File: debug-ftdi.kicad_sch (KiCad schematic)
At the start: 116 parts, among them J3 USB-C_USB4105-GF-A, J4 HDMI-A_WE_685119134923, J5 MicroSD_693071020811, Q4 BSS138PW, Q5 BSS138PW, Q6 BSS138PW, Q7 BSS138PW, Q8 BSS138PW, U10 TPD4E05U06QDQARQ1, U11 TPD4E05U06QDQARQ1, U12 TPD4E05U06QDQARQ1, U13 TXU0304BQAR, U14 TPD4E05U06QDQARQ1, U5 NCP718BSN330T1G, U6 FT4232H_VQFN, U7 TXU0304BQAR, U8 TPD4E05U06QDQARQ1, U9 SN74HC595B, Y1 Resonator_12MHz_ABM8G

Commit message: Finish creating hierarchical buses and structure, start reconnecting signals
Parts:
- removed C126: C_10u_6.3V_0402, sodimm-ddr5-tester-footprints:C_0402_1005Metric, symbol sodimm-ddr5-tester:C_10u_6.3V_0402
- removed C129: C_1u_0402, sodimm-ddr5-tester-footprints:C_0402_1005Metric, symbol sodimm-ddr5-tester:C_1u_0402
- removed C132: C_100n_0402, sodimm-ddr5-tester-footprints:C_0402_1005Metric, symbol sodimm-ddr5-tester:C_100n_0402
- removed D14: BAT54-02V-G3-08, sodimm-ddr5-tester-footprints:SOD-523, symbol sodimm-ddr5-tester:BAT54-02V-G3-08
- removed D4, D5, D6, D7, D8: LED_G_0603_KP-1608CGCK, sodimm-ddr5-tester-footprints:LED_0603_1608Metric_G, symbol sodimm-ddr5-tester:LED_G_0603_KP-1608CGCK
- removed FB3: FB_120Z_2A_Murata-BLM18PG_0603, sodimm-ddr5-tester-footprints:FB_0603_1608Metric, symbol sodimm-ddr5-tester:FB_120Z_2A_Murata-BLM18PG_0603
- removed J4: HDMI-A_WE_685119134923, sodimm-ddr5-tester-footprints:HDMI-A_Receptacle_WE_685119134923, symbol sodimm-ddr5-tester:HDMI-A_WE_685119134923
- removed J5: MicroSD_693071020811, sodimm-ddr5-tester-footprints:MicroSD_Wurth_693071020811, symbol sodimm-ddr5-tester:MicroSD_693071020811
- removed Q4, Q5, Q6, Q7, Q8: BSS138PW, sodimm-ddr5-tester-footprints:SC70-3, symbol sodimm-ddr5-tester:BSS138PW
- removed R40, R41, R42, R45, R46, R84, R89: R_330R_0402, sodimm-ddr5-tester-footprints:R_0402_1005Metric, symbol sodimm-ddr5-tester:R_330R_0402
- removed R70, R71, R72, R73, R74, R75, R76, R77: R_0R_0402, sodimm-ddr5-tester-footprints:R_0402_1005Metric, symbol sodimm-ddr5-tester:R_0R_0402
- removed R80, R81, R82, R83, R85, R86, R87: R_20k_0402, sodimm-ddr5-tester-footprints:R_0402_1005Metric, symbol sodimm-ddr5-tester:R_20k_0402
- removed TP2, TP3, TP4, TP5, TP6: TP_1mm_SMD, sodimm-ddr5-tester-footprints:TP_SMD_1mm, symbol sodimm-ddr5-tester:TP_1mm_SMD
- removed U10, U11, U12, U14: TPD4E05U06QDQARQ1, sodimm-ddr5-tester-footprints:USON-10_2.5x1mm_P0.5mm, symbol sodimm-ddr5-tester:TPD4E05U06QDQARQ1
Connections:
- no-connect marks 30 -> 28
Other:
- note added: "Debug FTDI"
- note removed: "Debug UART"
- note removed: "HDMI"
- note removed: "SD card"
- note removed: "User LEDs"
- moved on the sheet: C109, C110, C111, C112, C113, C114, C115, C116, C117, C118, C119, C120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

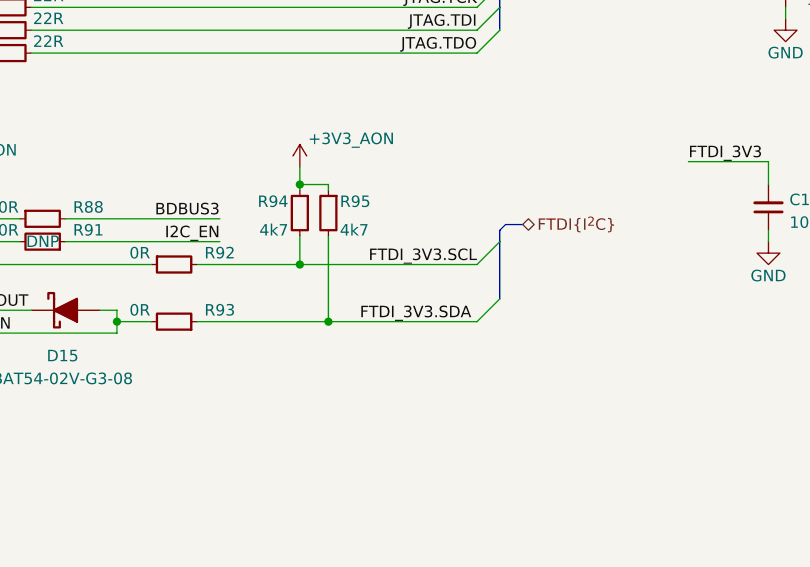
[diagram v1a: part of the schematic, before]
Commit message: Finish reconnecting signals after migration to the hierarchical structure
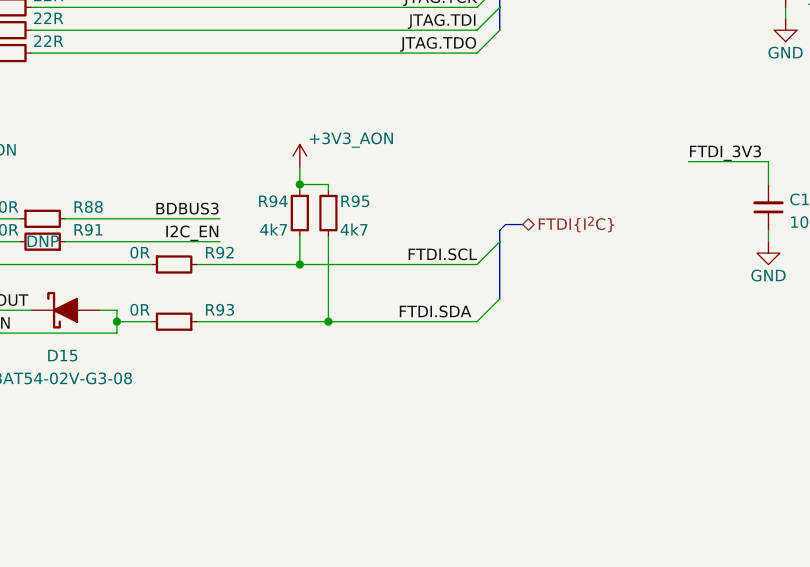
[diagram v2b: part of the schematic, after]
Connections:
- net FTDI_3V3.SCL renamed FTDI.SCL
- net FTDI_3V3.SDA renamed FTDI.SDA

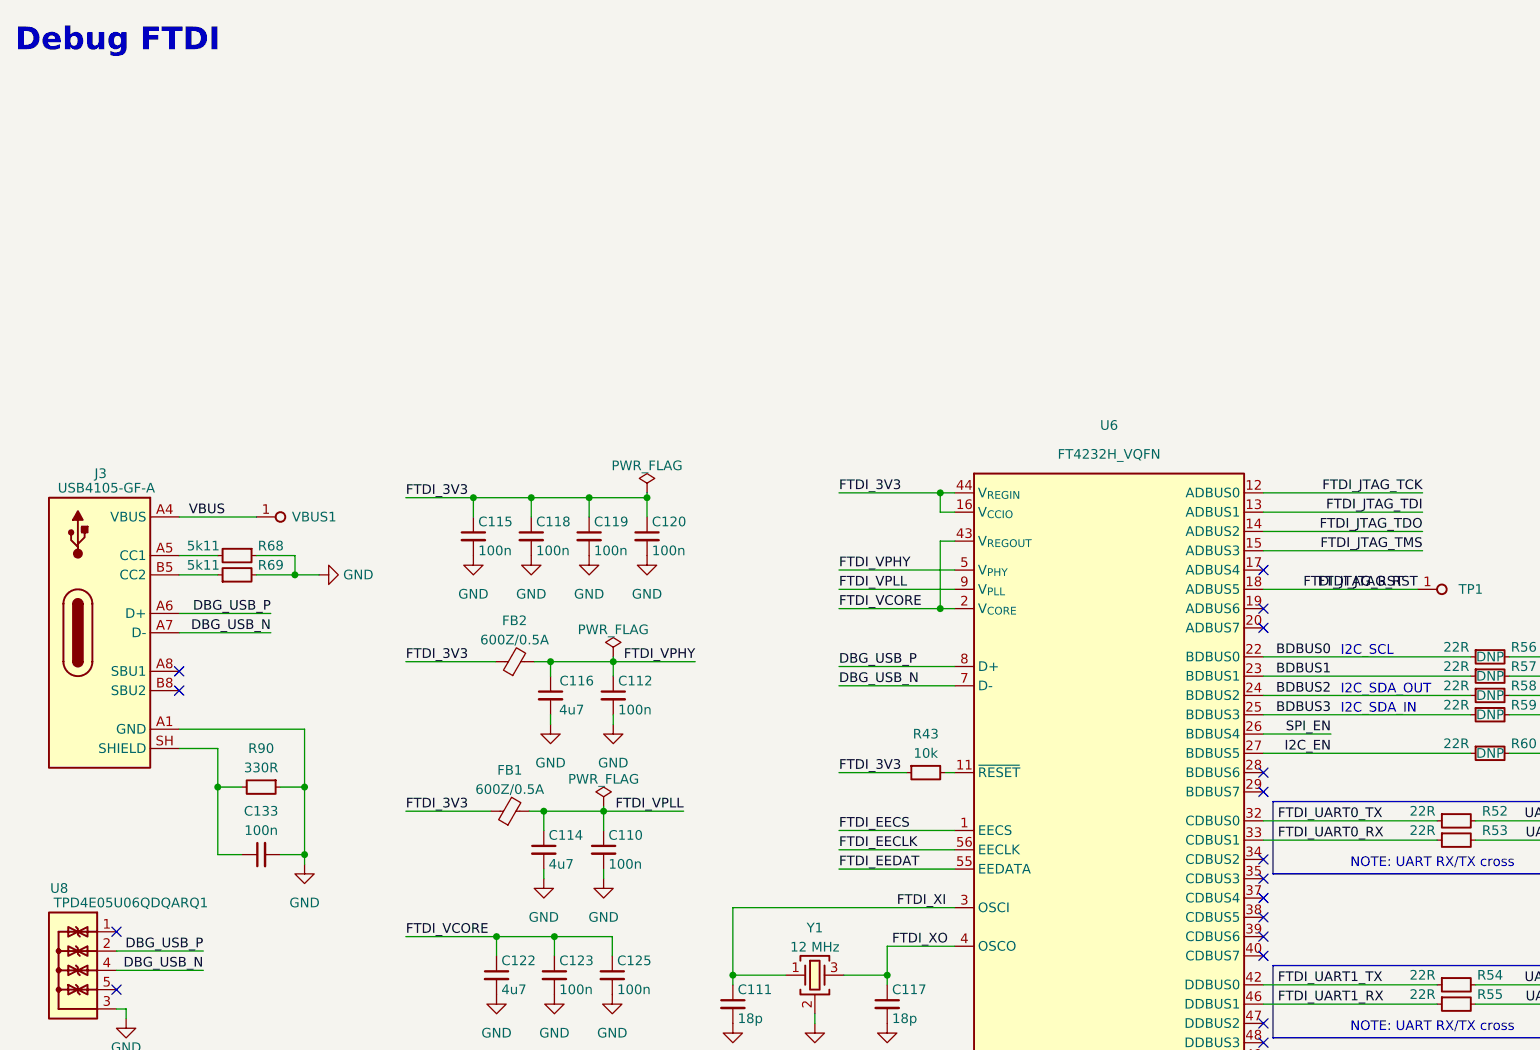
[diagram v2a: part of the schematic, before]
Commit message: Manually replace conflicted globlib files
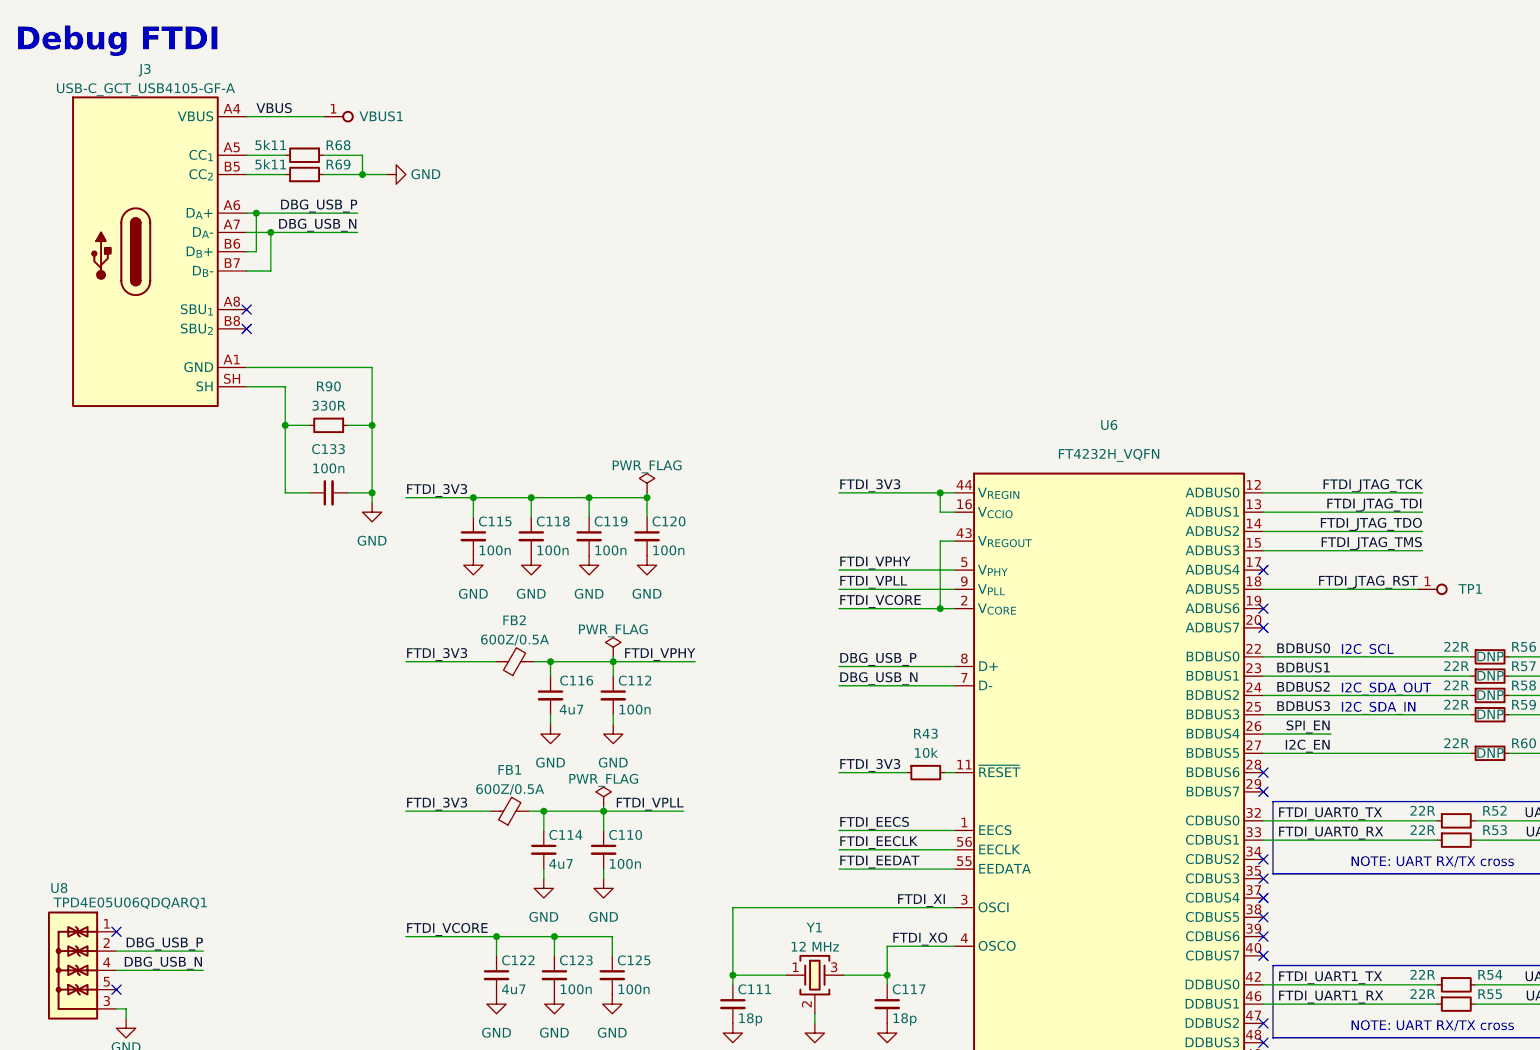
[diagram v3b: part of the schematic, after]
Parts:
- removed J3: USB-C_USB4105-GF-A, sodimm-ddr5-tester-footprints:USB-C_GCT_USB4105-GF-A, symbol sodimm-ddr5-tester:USB-C_USB4105-GF-A
- added J3: USB-C_GCT_USB4105-GF-A, antmicro-footprints:USB-C_Receptacle_GCT_USB4105-GF-A, symbol antmicroUSBConnectors:USB-C_GCT_USB4105-GF-A
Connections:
- net DBG_USB_N: now also J3.A7 (D_{A}-), J3.B7 (D_{B}-)
- net DBG_USB_P: now also J3.A6 (D_{A}+), J3.B6 (D_{B}+)
- net GND: now also J3.A1 (GND), J3.A12 (GND), J3.B1 (GND), J3.B12 (GND)
- net VBUS: now also J3.A4 (VBUS), J3.A9 (VBUS), J3.B4 (VBUS), J3.B9 (VBUS)
- net at R68.2: now also J3.A5 (CC_{1})
- net at R69.1: now also J3.B5 (CC_{2})
- net at C133.1, R90.2: now also J3.SH
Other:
- moved on the sheet: C133, R68, R69, R90, VBUS1

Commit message: Loclib of the project
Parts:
- FB1, FB2: footprint antmicro-footprints:FB_0603_1608Metric -> sodimm-ddr5-tester-footprints:FB_0603_1608Metric; symbol antmicroFerriteBeadsandChips:FB_600Z_0.5A_Murata-BLM18AG_0603 -> sodimm-ddr5-tester:FB_600Z_0.5A_Murata-BLM18AG_0603
- J3: footprint antmicro-footprints:USB-C_Receptacle_GCT_USB4105-GF-A -> sodimm-ddr5-tester-footprints:USB-C_Receptacle_GCT_USB4105-GF-A; symbol antmicroUSBConnectors:USB-C_GCT_USB4105-GF-A -> sodimm-ddr5-tester:USB-C_GCT_USB4105-GF-A
- U13: footprint sodimm-ddr5-tester-footprints:DHVQFN-14_1EP_2.5x3mm -> sodimm-ddr5-tester-footprints:DHVQFN-14-1EP_2.5x3mm
- Y1: footprint antmicro-footprints:Oscillator_SMD_Geyer_KX-7-4Pin_3.2x2.5mm -> sodimm-ddr5-tester-footprints:Oscillator_SMD_Geyer_KX-7-4Pin_3.2x2.5mm; symbol antmicroResonators:Resonator_12MHz_ABM8G -> sodimm-ddr5-tester:Resonator_12MHz_ABM8G

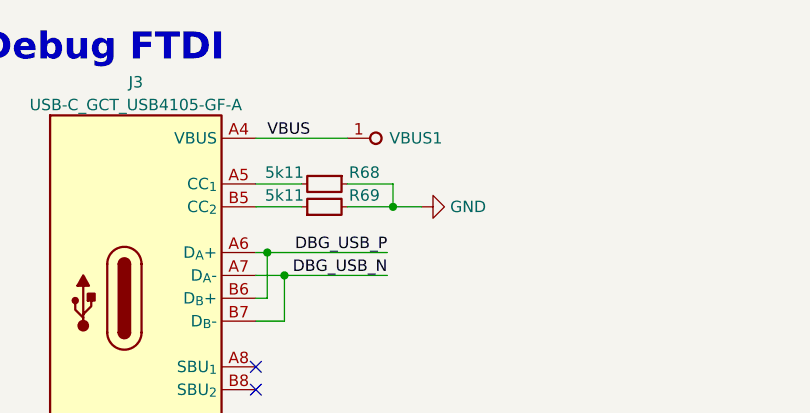
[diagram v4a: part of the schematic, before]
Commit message: Finish updating components to newest versions, improve silkscreen marking, bump revision
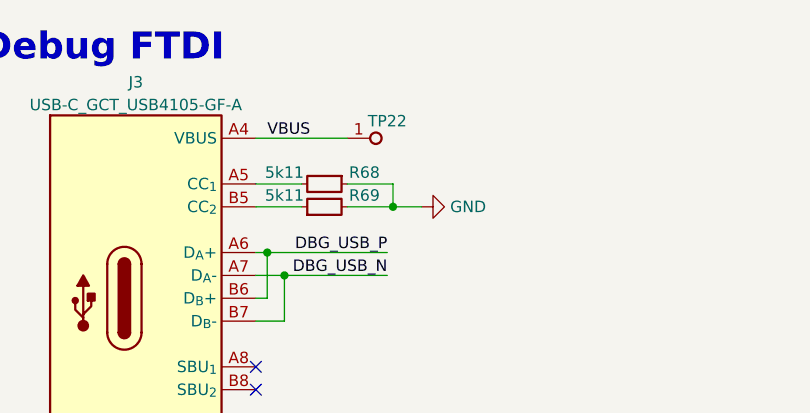
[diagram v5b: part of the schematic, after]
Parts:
- U7: footprint sodimm-ddr5-tester-footprints:DHVQFN-14_1EP_2.5x3mm -> sodimm-ddr5-tester-footprints:DHVQFN-14-1EP_2.5x3mm
- renumbered VBUS1 to TP22
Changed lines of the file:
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@@
     (title_block
         (title "SO-DIMM DDR5 Tester")
-        (date "2024-01-10")
-        (rev "1.1.0")
+        (date "2024-01-18")
+        (rev "1.1.1")
         (company "Antmicro Ltd.")
         (comment 1 "www.antmicro.com")
         (comment 2 "Antmicro Ltd"))
-    (bus_alias "SDIO"
-        (members "DAT[0..3]" "CMD" "CLK" "CD"))
-    (bus_alias "TMDS"
-        (members "D0_P" "D0_N" "D1_P" "D1_N" "D2_P" "D2_N" "CLK_P" "CLK_N"))
-    (bus_alias "USB"
-        (members "D+"))
     (junction
         (at 136.398 93.98)
@@
                     (size 1.27 1.27)
                     (thickness 0.15))))
-        (property "Footprint" "sodimm-ddr5-tester-footprints:DHVQFN-14_1EP_2.5x3mm"
+        (property "Footprint" "sodimm-ddr5-tester-footprints:DHVQFN-14-1EP_2.5x3mm"
             (id 2)
             (at 300.355 74.93 0)
@@
         (in_bom yes)
         (on_board yes)
-        (property "Reference" "VBUS1"
+        (property "Reference" "TP22"
             (id 0)
-            (at 62.865 29.21 0))
+            (at 59.69 27.305 0))
         (property "Value" "TP_1mm_SMD"
             (id 1)

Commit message: Finish schematic cleanup
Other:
- moved on the sheet: C109, C110, C111, C112, C113, C114, C115, C116, C117, C118, C119, C120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

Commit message: Clean schematic DRC
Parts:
- C111, C117: MPN MC0402N180J500CT -> CL05C180JB51PNC; Manufacturer Multicomp -> Samsung Electro-Mechanics
- U6: Manufacturer FTDI -> FTDI Chip
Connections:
- net SPI_EN: no longer names the net of U6.26 (BDBUS4)
- no-connect marks 28 -> 29
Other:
- note added: "SPI_EN"

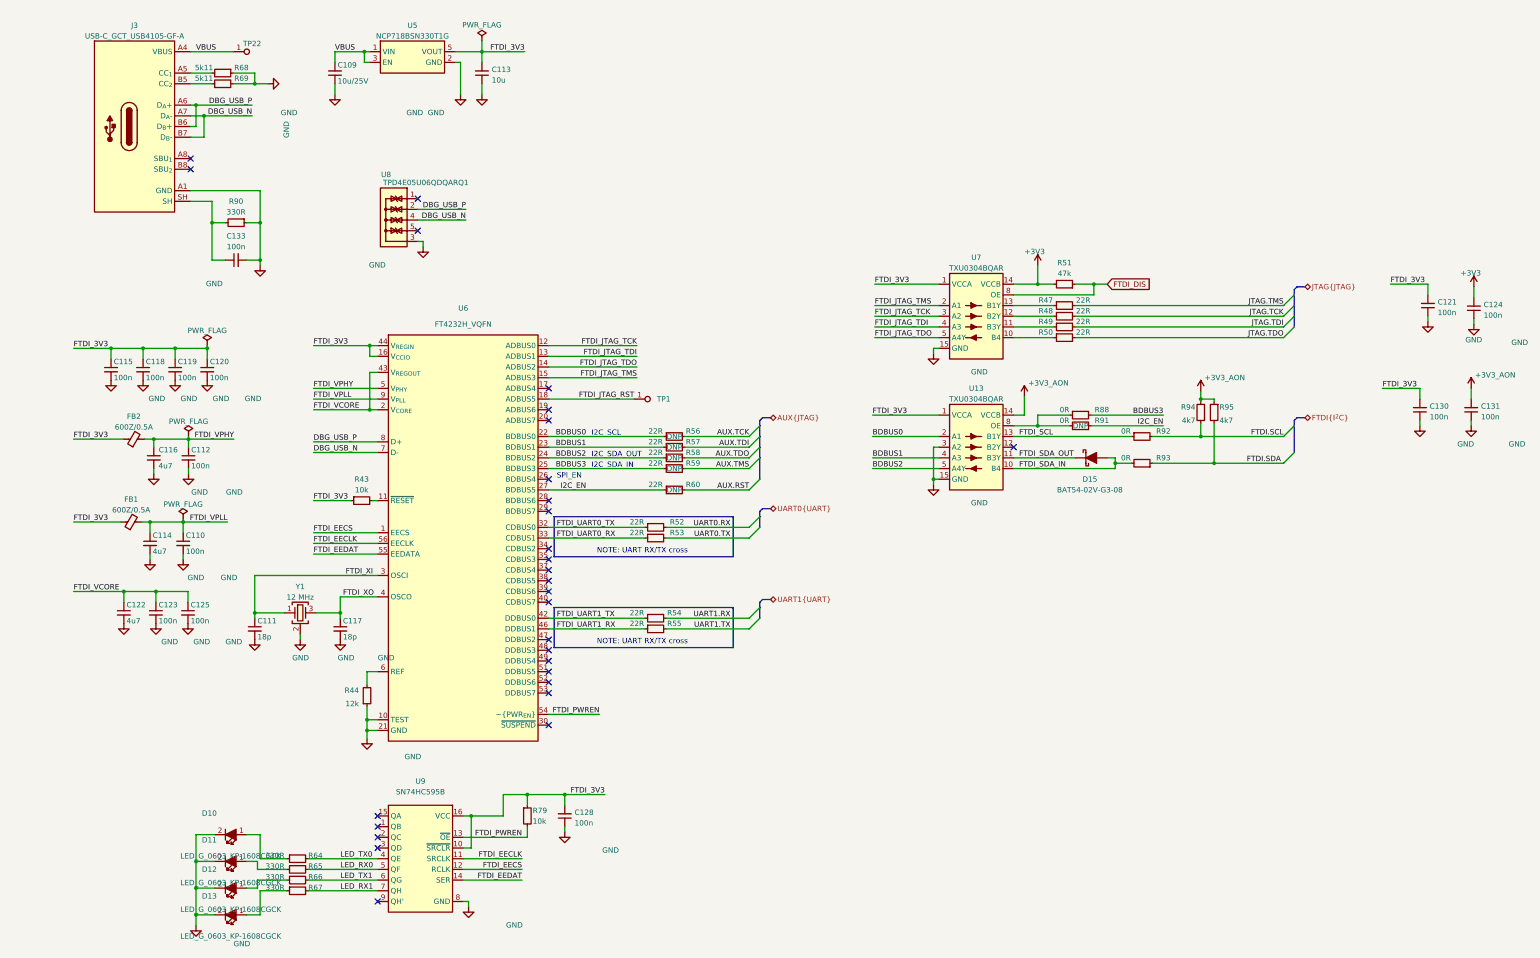
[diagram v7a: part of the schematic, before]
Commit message: Add updated components to local library
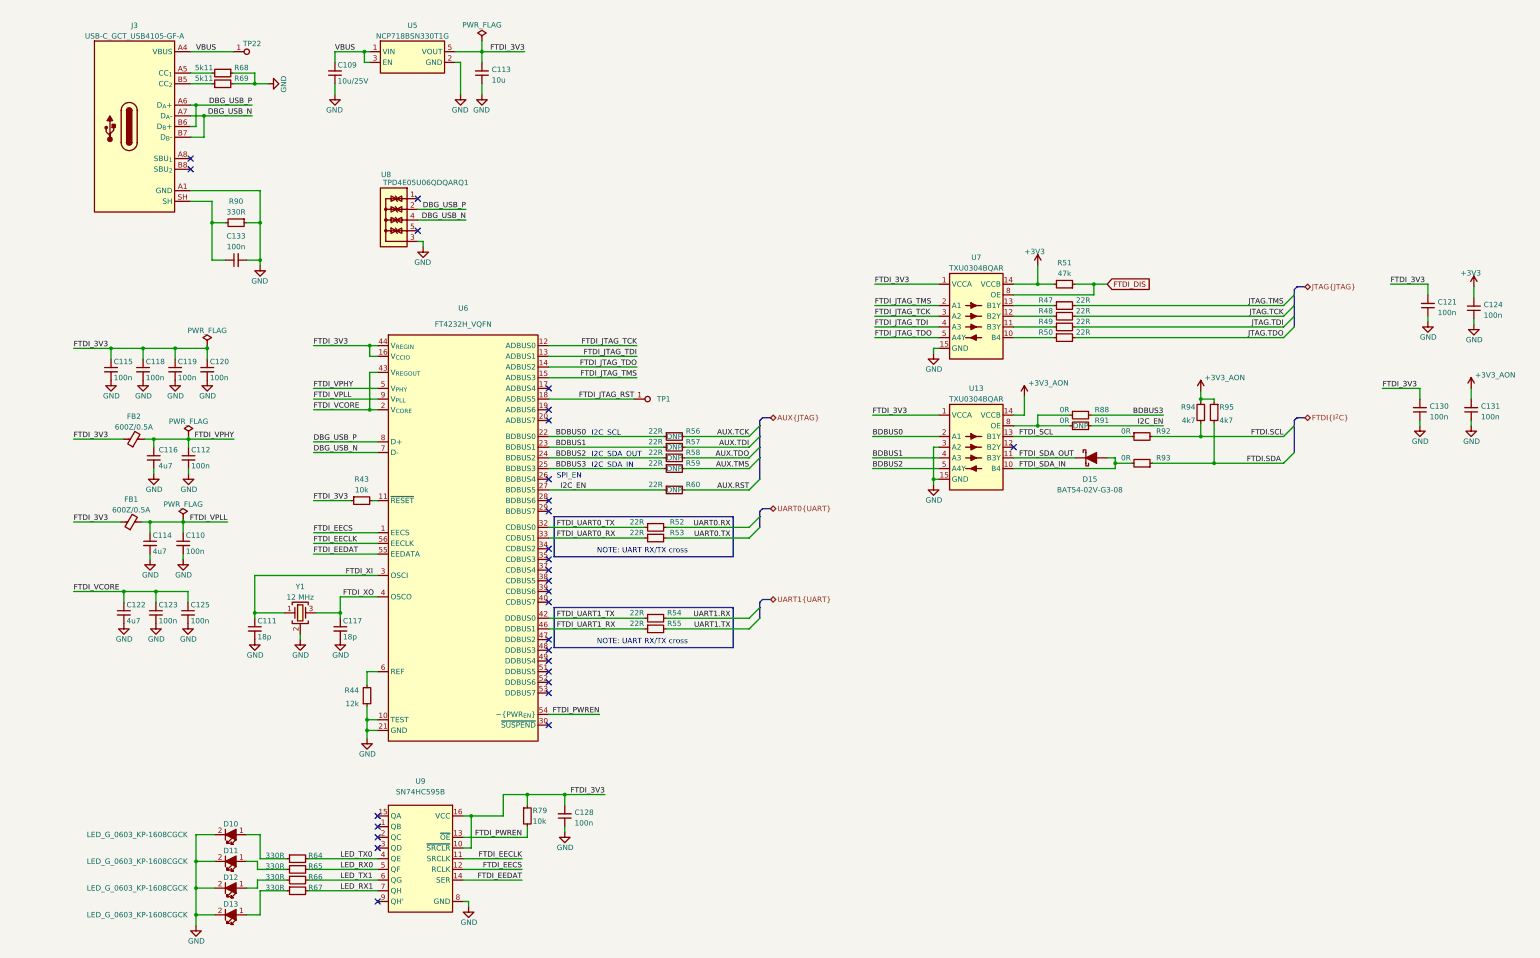
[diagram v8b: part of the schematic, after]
